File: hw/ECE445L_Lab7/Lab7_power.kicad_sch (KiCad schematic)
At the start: 9 parts, among them J1 JST1.25, J5 ZX62D-B-5PA8_30_, J6 Header2, U5 LP2950-33LPRE3

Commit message: mostly finished schem
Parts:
- removed +3.3V1: +3.3V, ECE445L:Testpoint_1x02_P2.54mm, symbol ECE445L:Testpoint
- removed +5V1: +5V, ECE445L:Testpoint_1x02_P2.54mm, symbol ECE445L:Testpoint
- removed C3, C5: 4.7uF, ECE445L:CP_Radial_Tantal200mil, symbol ECE445L:C_Polarized
- removed GND1: GND, ECE445L:Testpoint_1x02_P2.54mm, symbol ECE445L:Testpoint
- removed J1: JST1.25, ECE445L:JST-1x02_1.25mm, symbol ECE445L:JST1.25
- removed J5: ZX62D-B-5PA8_30_, ECE445L:ZX62DB5PA830, symbol ECE445L:ZX62D-B-5PA8_30_
- removed J6: Header2, ECE445L:PinHeader_1x02_P2.54mm_Vertical, symbol ECE445L:Header_2
- removed U5: LP2950-33LPRE3, ECE445L:TL431CLPM, symbol ECE445L:LP2950-33LPRE3
- added C3, C5, C8: C, symbol Device:C
- added C4, C6: 4.7u, Capacitor_SMD:C_0805_2012Metric_Pad1.18x1.45mm_HandSolder, symbol Device:C
- added J_{USB-C}: Conn_01x02, symbol Connector_Generic:Conn_01x02
- added L1: L, symbol Device:L
- added L2: L_Coupled, symbol Device:L_Coupled
- added U3: RBT05W24S12, Converter_DCDC:Converter_DCDC_TRACO_TSR0.5-24xx_TSR0.5-24xxx_THT, symbol Converter_DCDC:TSR0.5-2433
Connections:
- net +3V3: now also C6.1, U3.3 (Vout)
- net GND: now also C3.2, C4.2, C5.2, C6.2, J_{USB-C}.1 (Pin_1), L2.3, U3.2 (GND)
- new net: C3.1, L1.2, L2.1
- new net: C8.1, L2.2
- new net +20V: C4.1, C5.1, J_{USB-C}.2 (Pin_2), L1.1, U3.1 (Vin)
- new net GNDPWR: C8.2, L2.4
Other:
- note added: "+12V"
- note added: "+3V3"
- note added: "What do we use for 12V power delivery?"

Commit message: during lab sesh edits
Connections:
- net +20V is gone; now on net +12V: C4.1, C5.1, J_{USB-C}.2 (Pin_2), L1.1, U3.1 (Vin)
- net +12V: now also C8.1, L2.2
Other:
- note removed: "What do we use for 12V power delivery?"
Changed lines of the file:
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@@
-	)
-	(rectangle
-		(start 140.335 126.365)
-		(end 164.465 135.89)
-		(stroke
-			(width 0)
-			(type solid)
-		)
-		(fill
-			(type none)
-		)
 	)
 	(rectangle
@@
 		)
 	)
-	(text "What do we use for \n12V power delivery?"
-		(exclude_from_sim no)
-		(at 152.4 130.81 0)
-		(effects
-			(font
-				(size 1.27 1.27)
-			)
-		)
-	)
 	(junction
 		(at 132.715 106.045)
@@
 	)
 	(junction
-		(at 133.985 125.095)
+		(at 133.985 125.73)
 		(diameter 0)
 		(color 0 0 0 0)
@@
 	(wire
 		(pts
-			(xy 129.54 125.095) (xy 133.985 125.095)
+			(xy 129.54 125.73) (xy 133.985 125.73)
 		)
 		(stroke
@@
 	(wire
 		(pts
-			(xy 133.985 137.16) (xy 168.91 137.16)
+			(xy 133.985 137.16) (xy 143.51 137.16)
 		)
 		(stroke
@@
 	(wire
 		(pts
-			(xy 133.985 127.635) (xy 133.985 125.095)
+			(xy 133.985 125.73) (xy 144.78 125.73)
+		)
+		(stroke
+			(width 0)
+			(type default)
+		)
+	)
+	(wire
+		(pts
+			(xy 133.985 127.635) (xy 133.985 125.73)
 		)
 		(stroke
@@
 	(wire
 		(pts
-			(xy 129.54 128.905) (xy 129.54 125.095)
+			(xy 129.54 128.905) (xy 129.54 125.73)
 		)
 		(stroke
@@
 	(wire
 		(pts
-			(xy 133.985 125.095) (xy 138.43 125.095)
-		)
-		(stroke
-			(width 0)
-			(type default)
-		)
-	)
-	(wire
-		(pts
 			(xy 111.125 125.095) (xy 119.38 125.095)
 		)
@@
 	(wire
 		(pts
-			(xy 168.91 137.16) (xy 168.91 139.065)
+			(xy 143.51 137.16) (xy 143.51 139.7)
 		)
 		(stroke
@@
 		)
 	)
-	(label "+20V"
+	(label "+12V"
 		(at 88.265 125.095 0)
 		(effects
@@
 		)
 	)
-	(label "+20V"
+	(label "+12V"
 		(at 110.49 95.885 0)
 		(effects
@@
 	(global_label "+12V"
 		(shape output)
-		(at 168.91 125.095 0)
+		(at 144.78 125.73 0)
 		(fields_autoplaced yes)
 		(effects
@@
 		)
 		(property "Intersheetrefs" "${INTERSHEET_REFS}"
-			(at 176.9752 125.095 0)
+			(at 152.8452 125.73 0)
 			(hide yes)
 			(show_name no)
@@
 	(symbol
 		(lib_id "power:GNDPWR")
-		(at 168.91 139.065 0)
+		(at 143.51 139.7 0)
 		(unit 1)
 		(body_style 1)
@@
 		(fields_autoplaced yes)
 		(property "Reference" "#PWR030"
-			(at 168.91 144.145 0)
+			(at 143.51 144.78 0)
 			(hide yes)
 			(show_name no)
@@
 		)
 		(property "Value" "GNDPWR"
-			(at 168.783 142.875 0)
+			(at 143.383 143.51 0)
 			(show_name no)
 			(do_not_autoplace no)
@@
 		)
 		(property "Footprint" ""
-			(at 168.91 140.335 0)
+			(at 143.51 140.97 0)
 			(hide yes)
 			(show_name no)
@@
 		)
 		(property "Datasheet" ""
-			(at 168.91 140.335 0)
+			(at 143.51 140.97 0)
 			(hide yes)
 			(show_name no)
@@
 		)
 		(property "Description" "Power symbol creates a global label with name \"GNDPWR\" , global ground"
-			(at 168.91 139.065 0)
+			(at 143.51 139.7 0)
 			(hide yes)
 			(show_name no)
@@
 		)
 	)
-	(group ""
-		(members "2fef0c20-fdd8-456b-8507-faa052da9596" "eb2af501-ddd8-41b7-8d65-fb183a1be364")
-	)
 )

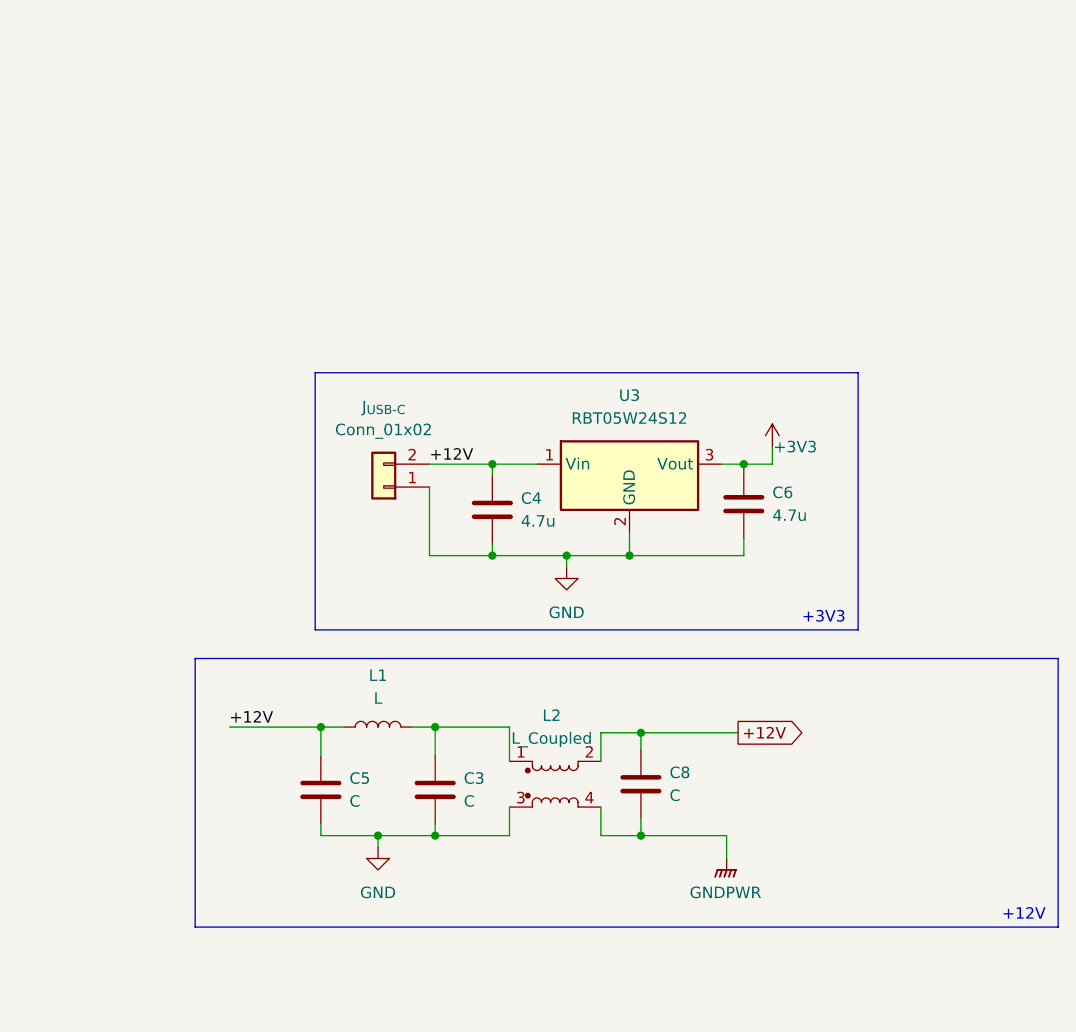
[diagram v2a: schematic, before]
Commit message: added reverse engineering for water atomizer
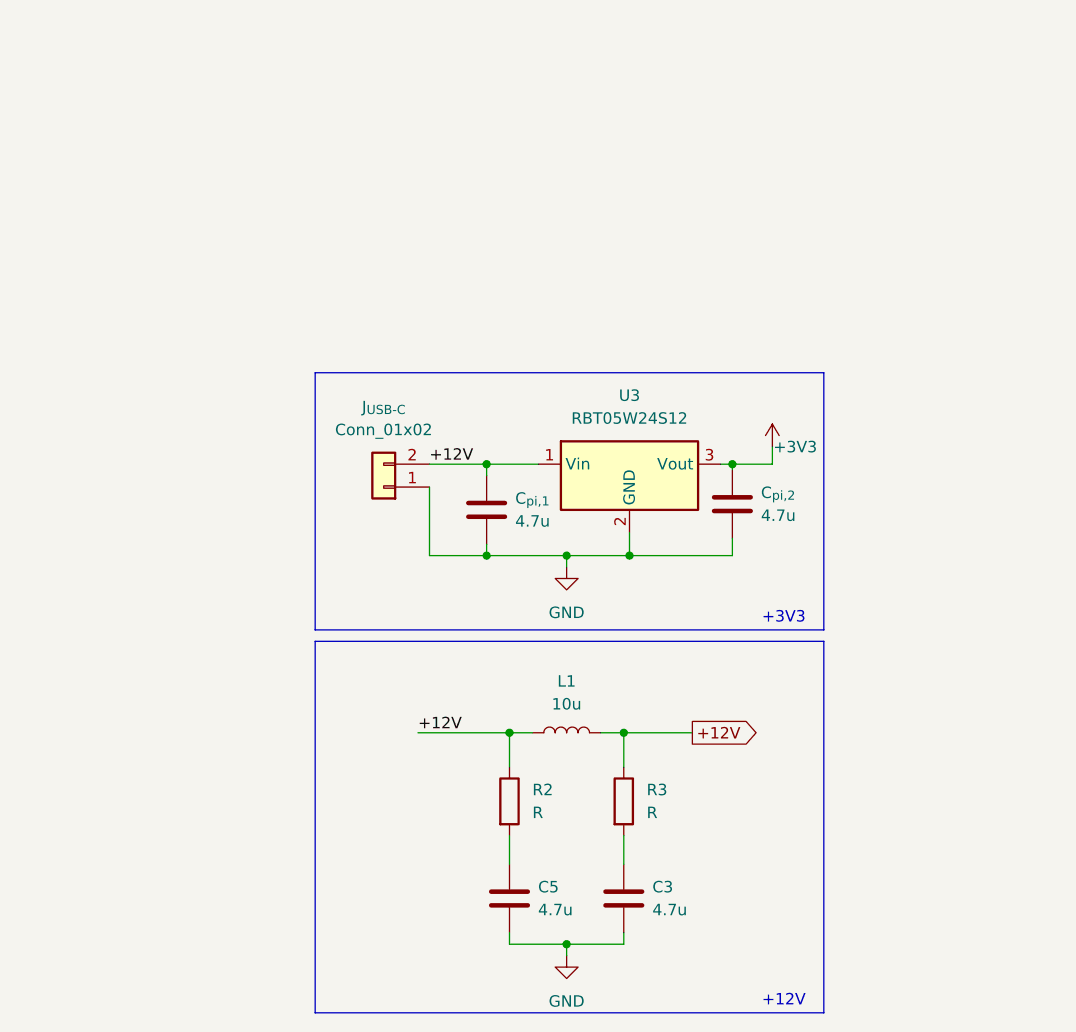
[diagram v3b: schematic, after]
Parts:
- removed C8: C, symbol Device:C
- removed L2: L_Coupled, symbol Device:L_Coupled
- added R2, R3: R, symbol Device:R
- C3, C5: value C -> 4.7u
- L1: value L -> 10u
- renumbered C4 to C_{pi,1}, C6 to C_{pi,2}
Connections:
- net +12V: now also L1.2, R2.1, R3.1; no longer C5.1
- net at C3.1: now also R3.2; no longer L1.2
- new net: C5.1, R2.2
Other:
- company: (none) -> ECE445L
- moved on the sheet: C3, C5, C_{pi,1}, C_{pi,2}, L1

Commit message: almost finished with schem
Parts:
- removed C5: 4.7u, symbol Device:C
- removed R2: R, symbol Device:R
- added F1: Fuse, symbol Device:Fuse
- added TP_{12V}, TP_{3V3}: TestPoint, TestPoint:TestPoint_Bridge_Pitch2.0mm_Drill0.7mm, symbol Connector:TestPoint
- C3: value 4.7u -> 1200u
- L1: footprint (none) -> Inductor_SMD:L_APV_APH1040
- R_{filter}: renamed from R3; value R -> 0.25; footprint (none) -> Resistor_SMD:R_0603_1608Metric_Pad0.98x0.95mm_HandSolder
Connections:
- net +12V: now also F1.2, TP_{12V}.1; no longer J_{USB-C}.2 (Pin_2)
- net +3V3: now also TP_{3V3}.1
- new net: F1.1, J_{USB-C}.2 (Pin_2)
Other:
- note added: "Test Points"
- moved on the sheet: C3, J_{USB-C}, L1, R_{filter}

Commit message: finished prelim schem
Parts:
- 12V1: renamed from TP_{12V}; footprint TestPoint:TestPoint_Bridge_Pitch2.0mm_Drill0.7mm -> TestPoint:TestPoint_Keystone_5010-5014_Multipurpose
- 3V3: renamed from TP_{3V3}; footprint TestPoint:TestPoint_Bridge_Pitch2.0mm_Drill0.7mm -> TestPoint:TestPoint_Keystone_5010-5014_Multipurpose
- C_{filter}1: renamed from C3; footprint (none) -> Capacitor_THT:CP_Radial_D10.0mm_P5.00mm; symbol Device:C -> Device:C_Polarized; Distributor (none) -> Mouser; Manufacturer (none) -> KEMET; Manufacturer_Name (none) -> KEMET; Manufacturer_Part_Number (none) -> A7D0MW128M1EAAS011; Mouser Part Number (none) -> 80-A7D0MW128M1EAAS11
- C_{pi}1: renamed from C_{pi,1}; footprint Capacitor_SMD:C_0805_2012Metric_Pad1.18x1.45mm_HandSolder -> Capacitor_SMD:C_0603_1608Metric_Pad1.08x0.95mm_HandSolder; Distributor (none) -> Mouser; Manufacturer (none) -> Walsin; Manufacturer_Part_Number (none) -> 0805X475M250CT; Mouser Part Number (none) -> 791-0805X475M250CT
- C_{pi}2: renamed from C_{pi,2}; footprint Capacitor_SMD:C_0805_2012Metric_Pad1.18x1.45mm_HandSolder -> Capacitor_SMD:C_0603_1608Metric_Pad1.08x0.95mm_HandSolder; Distributor (none) -> Mouser; Manufacturer (none) -> Walsin; Manufacturer_Part_Number (none) -> 0805X475M250CT; Mouser Part Number (none) -> 791-0805X475M250CT
- F1: footprint (none) -> Fuse:Fuseholder_Cylinder-5x20mm_Wuerth_696103101002-SMD_Horizontal_Open
- J_{USB-C}1: renamed from J_{USB-C}; footprint (none) -> Connector_PinHeader_2.54mm:PinHeader_1x02_P2.54mm_Vertical
- L_{filter}1: renamed from L1; value 10u -> 10uH; footprint Inductor_SMD:L_APV_APH1040 -> Inductor_SMD:L_Coilcraft_MSS1038-XXX; Distributor (none) -> Mouser; Manufacturer (none) -> Pulse Electronics; Manufacturer_Part_Number (none) -> AMRM00101040100MA1; Mouser Part Number (none) -> 673-AMRM101040100MA1
- R_{filter}1: renamed from R_{filter}; Distributor (none) -> Mouser; Manufacturer (none) -> YAGEO; Manufacturer_Part_Number (none) -> RL0603JR-070R25L; Mouser Part Number (none) -> 603-RL0603JR-070R25L
- U_{3V3DC}1: renamed from U3; Distributor (none) -> Mouser; Manufacturer (none) -> XP Power; Manufacturer_Part_Number (none) -> RBT05W24S3V3; Mouser Part Number (none) -> 209-RBT05W24S3V3
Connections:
- net +12V: no longer C_{pi}1.1, F1.2, L_{filter}1.1, U_{3V3DC}1.1 (Vin)
- net V_{in,fused}: now reaches F1.1
- net V_{in,fused}: now also C_{pi}1.1, L_{filter}1.1, U_{3V3DC}1.1 (Vin); no longer J_{USB-C}1.2 (Pin_2)
- new net V_{in}: F1.2, J_{USB-C}1.2 (Pin_2)
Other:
- moved on the sheet: F1

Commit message: started pcb layout
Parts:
- F1: footprint Fuse:Fuseholder_Cylinder-5x20mm_Wuerth_696103101002-SMD_Horizontal_Open -> ECE445L:WR-FSH_THT_2
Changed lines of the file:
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@@
-		)
-	)
-	(text_box "TODO: Find footprint for fuse holder"
-		(exclude_from_sim no)
-		(at 99.06 97.155 0)
-		(size 14.605 8.0376)
-		(margins 0.9525 0.9525 0.9525 0.9525)
-		(stroke
-			(width 0)
-			(type solid)
-		)
-		(fill
-			(type none)
-		)
-		(effects
-			(font
-				(size 1.27 1.27)
-			)
-			(justify left top)
 		)
 	)
@@
 			)
 		)
-		(property "Footprint" "Fuse:Fuseholder_Cylinder-5x20mm_Wuerth_696103101002-SMD_Horizontal_Open"
+		(property "Footprint" "ECE445L:WR-FSH_THT_2"
 			(at 104.775 94.107 90)
 			(hide yes)
@@
 			)
 		)
-		(property "Datasheet" ""
+		(property "Datasheet" "https://www.we-online.com/components/products/datasheet/696108003002.pdf"
 			(at 104.775 95.885 0)
 			(hide yes)

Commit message: handoff to jonathan until midnight
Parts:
- C_{pi}1, C_{pi}2: Distributor Mouser -> Valvano
- U_{3V3DC}1: footprint Converter_DCDC:Converter_DCDC_TRACO_TSR0.5-24xx_TSR0.5-24xxx_THT -> ECE445L:N78032C
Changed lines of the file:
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@@
 			)
 		)
-		(property "Distributor" "Mouser"
+		(property "Distributor" "Valvano"
 			(at 116.84 100.965 0)
 			(hide yes)
@@
 			)
 		)
-		(property "Distributor" "Mouser"
+		(property "Distributor" "Valvano"
 			(at 144.145 100.33 0)
 			(hide yes)
@@
 			)
 		)
-		(property "Footprint" "Converter_DCDC:Converter_DCDC_TRACO_TSR0.5-24xx_TSR0.5-24xxx_THT"
+		(property "Footprint" "ECE445L:N78032C"
 			(at 132.715 104.521 0)
 			(hide yes)
